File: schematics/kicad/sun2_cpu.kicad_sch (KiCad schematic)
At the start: 9 parts, among them U100 MC68010, U111 74F251, U115 74F04, U119 74LS148, U120 8211

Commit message: Substantial work on first page/CPU
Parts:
- added C100: C, symbol Device:C
- added R100, R102: 16k, symbol Device:R_US
- added R101: 100k, symbol Device:R_US
- added R103: 6.8k, symbol Device:R_US
- added U102: 74F00, Package_DIP:DIP-14_W7.62mm, symbol sun2:74F00
- added U109: 74F08, Package_DIP:DIP-14_W7.62mm, symbol sun2:74F08
- added U110: 7407, Package_DIP:DIP-14_W7.62mm, symbol sun2:7407
- added U114: 74LS20, symbol 74xx:74LS20
- added U122: 7406, Package_DIP:DIP-14_W7.62mm, symbol sun2:7406
- added U206: 74F74, Package_DIP:DIP-14_W7.62mm, symbol sun2:74F74
- added U608, U610: 74LS04, symbol sun2:74LS04
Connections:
- net P.D4: now reaches U100.1 (D4)
- net P.DTACK\: now reaches U100.10 (~{DTACK})
- net P.DTACK\: now also U111.6 (W)
- net P.BG\: now reaches U100.11 (~{BG})
- net P.BACK\: now reaches U100.12 (~{BGACK})
- net P.BR\: now reaches U100.13 (~{BR})
- net VCC: now reaches U100.14 (V_{CC})
- net VCC: now also S100.1 (common), S103.1 (common), S104.1 (common), S105.1 (common), U100.49 (V_{CC}), U119.16 (VCC), U120.8 (VCC), R100.1, U206.1 (~{R})
- net C(100.0-50): now reaches U100.15 (CLK)
- net C(100.0-50): now also U206.3 (C)
- net GND: now reaches U100.16 (GND)
- net GND: now also U100.53 (GND), U119.10 (IO), U119.8 (GND), U120.5 (GND), C100.2, R103.2
- net P.HALT\: now reaches U100.17 (~{HALT})
- net P.HALT\: now also U110.2, U110.4
- net P.RESET\: now reaches U100.18 (~{RESET})
- net P.RESET\: now also U110.6, U608.9
- net P.D3: now reaches U100.2 (D3)
- net P.VPA\: now reaches U100.21 (~{VPA})
- net P.BERR\: now reaches U100.22 (~{BERR})
- net P.BERR\: now also U109.3
- net IPL2\: now reaches U100.23 (~{IPL2}), U119.6 (S2)
- net IPL1\: now reaches U100.24 (~{IPL1}), U119.7 (S1)
- net IPL0\: now reaches U100.25 (~{IPL0}), U119.9 (S0)
- net P.FC2: now reaches U100.26 (FC2)
- net P.FC2: now also S104.4 (R3)
- net P.FC1: now reaches U100.27 (FC1)
- net P.FC1: now also S104.3 (R2)
- net P.FC0: now reaches U100.28 (FC0)
- net P.FC0: now also S104.2 (R1)
- net P.A1: now reaches U100.29 (A1)
- net P.D2: now reaches U100.3 (D2)
- net P.A2: now reaches U100.30 (A2)
- net P.A3: now reaches U100.31 (A3)
- net P.A4: now reaches U100.32 (A4)
- net P.A5: now reaches U100.33 (A5)
- net P.A6: now reaches U100.34 (A6)
- net P.A7: now reaches U100.35 (A7)
- net P.A8: now reaches U100.36 (A8)
- net P.A9: now reaches U100.37 (A9)
- net P.A10: now reaches U100.38 (A10)
- net P.A11: now reaches U100.39 (A11)
- net P.A11: now also S104.10 (R9)
- net P.D1: now reaches U100.4 (D1)
- net P.A12: now reaches U100.40 (A12)
- net P.A12: now also S104.9 (R8)
- net P.A13: now reaches U100.41 (A13)
- net P.A13: now also S104.8 (R7)
- net P.A14: now reaches U100.42 (A14)
- net P.A14: now also S104.7 (R6)
- net P.A15: now reaches U100.43 (A15)
- net P.A15: now also S105.10 (R9)
- net P.A16: now reaches U100.44 (A16)
- net P.A16: now also S105.9 (R8)
- net P.A17: now reaches U100.45 (A17)
- net P.A17: now also S105.8 (R7)
- net P.A18: now reaches U100.46 (A18)
- net P.A18: now also S105.7 (R6)
- net P.A19: now reaches U100.47 (A19)
- net P.A19: now also S105.6 (R5)
- net P.A20: now reaches U100.48 (A20)
- net P.A20: now also S105.5 (R4)
- net P.D0: now reaches U100.5 (D0)
- net P.A21: now reaches U100.50 (A21)
- net P.A21: now also S105.4 (R3)
- net P.A22: now reaches U100.51 (A22)
- net P.A22: now also S105.3 (R2)
- net P.A23: now reaches U100.52 (A23)
- net P.A23: now also S105.2 (R1)
- net P.D15: now reaches U100.54 (D15)
- net P.D14: now reaches U100.55 (D14)
- net P.D13: now reaches U100.56 (D13)
- net P.D12: now reaches U100.57 (D12)
- net P.D11: now reaches U100.58 (D11)
- net P.D10: now reaches U100.59 (D10)
- net P.AS\: now reaches U100.6 (~{AS})
- net P.AS\: now also U111.7 (S), U115.1
- net P.D9: now reaches U100.60 (D9)
- net P.D8: now reaches U100.61 (D8)
- net P.D7: now reaches U100.62 (D7)
- net P.D6: now reaches U100.63 (D6)
- net P.D5: now reaches U100.64 (D5)
- net P.UDS\: now reaches U100.7 (~{UDS})
- net P.UDS\: now also U115.3, U109.5
- net P.LDS\: now reaches U100.8 (~{LDS})
- net P.LDS\: now also U115.5, U109.4
- net P.R/W\: now reaches U100.9 (R/~{W})
- net P.R/W\: now also U115.9
- net Q.AS\: now reaches U115.12
- net AS: now reaches U115.13
- net AS: now also U115.2
- net XACK: now reaches U115.10
- net XACK: now also U111.12 (D7), U111.13 (D6)
- net XACK\: now reaches U115.11
- net INT4\: now reaches U119.1 (I4)
- net INT4\: now also S100.6 (R5)
- net INT1\: now reaches U119.11 (I1)
- net INT1\: now also S100.3 (R2)
- net INT2\: now reaches U119.12 (I2)
- net INT2\: now also S100.4 (R3)
- net INT3\: now reaches U119.13 (I3)
- net INT3\: now also S100.5 (R4)
- net INT5\: now reaches U119.2 (I5)
- net INT5\: now also S100.7 (R6)
- net INT6\: now reaches U119.3 (I6)
- net INT6\: now also S100.8 (R7)
- net INT7\: now reaches U119.4 (I7)
- net INT7\: now also S100.2 (R1)
- net at U119.5 (EI): now also U608.12
- net C.S5: now reaches U111.1 (D3)
- net C.S5: now also U111.4 (D0)
- net TYPE1: now reaches U111.10 (B)
- net TYPE0: now reaches U111.11 (A)
- net IOACK: now reaches U111.14 (D5)
- net P2.WAIT\: now reaches U111.15 (D4)
- net P2.WAIT\: now also U122.4
- net C.S4: now reaches U111.9 (C)
- net LDS: now reaches U115.6
- net R\/W: now reaches U115.8
- net UDS: now reaches U115.4
- net POR\: now reaches S104.5 (R4)
- net POR\: now also U120.4 (OUT)
- net EN.PARGEN\: now reaches S104.6 (R5)
- net FPPERR\: now reaches S100.10 (R9)
- net INT.SCC\: now reaches S100.9 (R8)
- net at U120.2 (HYS): now also R101.2
- net at U120.3 (THR): now also R101.1, R102.2
- new net: C100.1, R100.2, R102.1, R103.1
- new net: U109.8, U122.3
- new net: U109.9, U610.12
- new net BERR: U206.6 (~{Q})
- new net BERR\: U109.1, U206.5 (Q)
- new net DS\: U109.6
- new net EN.INT: U608.13
- new net EN.S4: U102.13
- new net ERR: U102.12, U114.6
- new net ERR\: U102.11, U206.2 (D)
- new net INIT\: U110.3, U110.5
- new net OE.ROP\: U109.10
- new net P1.INIT\: U122.1, U608.8
- new net PARERRL\: U114.4
- new net PARERRU\: U114.5
- new net PROTERR\: U114.1
- new net RESET: U122.2
- new net ROPCYC\: U610.13
- new net TIMEOUT\: U114.2
- new net XBERR\: U109.2
- new net XHALT\: U110.1
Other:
- moved on the sheet: S100, U111A, U111B, U115A, U115B, U115C, U115D, U115E, U115F, U115G

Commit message: Finish first page/CPU
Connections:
- net C.S5: now also U111.2 (D2), U111.3 (D1)
- net FPPERR\: now also U110.13
- net INT.SCC\: now also U110.11
- net INT1\: now also U110.12, U122.8
- net INT2\: now also U122.10
- net INT3\: now also U122.12
- net INT6\: now also U110.10
- net P.AS\: now also S103.2 (R1)
- net P.BG\: now also S103.10 (R9)
- net P.DTACK\: now also S103.7 (R6)
- net P.HALT\: now also S103.6 (R5)
- net P.LDS\: now also S103.4 (R3)
- net P.RESET\: now also S103.8 (R7)
- net P.R/W\: now also S103.5 (R4)
- net P.UDS\: now also S103.3 (R2)
- net RESET: now also S103.9 (R8)
- net EN.INT2: now reaches U122.11
- net EN.INT3: now reaches U122.13
- net EN.INT1: now reaches U122.9
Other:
- note added: "BERR LOGIC"
- note added: "DTACK GENERATOR"
- note added: "INTERRUPT LOGIC"
- note added: "POWER-ON RESET"
- moved on the sheet: C100, R100, R101, R102, R103, S103, S104, S105, U100, U102D, U109A, U109B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

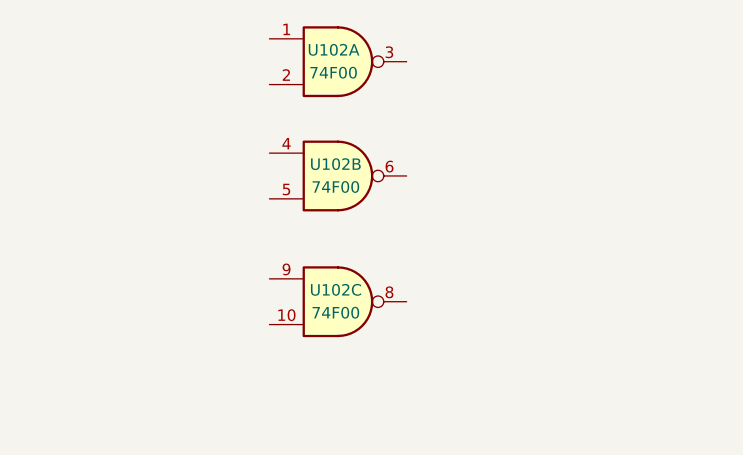
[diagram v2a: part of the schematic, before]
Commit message: System clock generator
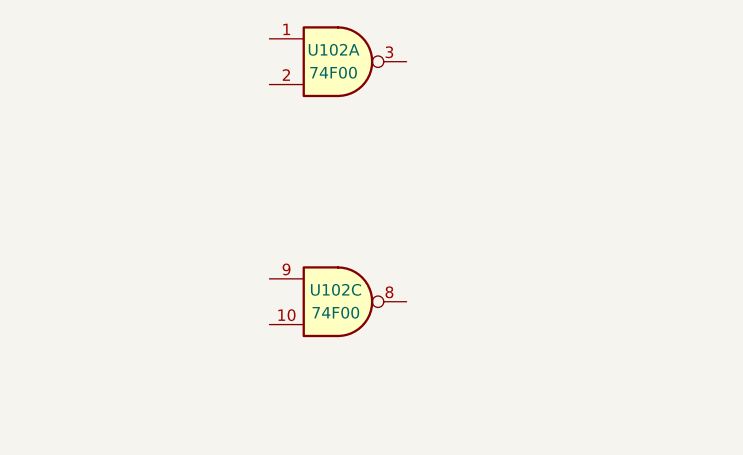
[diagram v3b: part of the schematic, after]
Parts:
- removed unit 2 of U102
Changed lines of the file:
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@@
-	)
-	(symbol
-		(lib_id "sun2:74F00")
-		(at -40.64 12.7 0)
-		(unit 2)
-		(exclude_from_sim no)
-		(in_bom yes)
-		(on_board yes)
-		(dnp no)
-		(property "Reference" "U102"
-			(at -40.894 11.43 0)
-			(effects
-				(font
-					(size 1.27 1.27)
-				)
-			)
-		)
-		(property "Value" "74F00"
-			(at -40.894 13.97 0)
-			(effects
-				(font
-					(size 1.27 1.27)
-				)
-			)
-		)
-		(property "Footprint" "Package_DIP:DIP-14_W7.62mm"
-			(at -40.64 12.7 0)
-			(effects
-				(font
-					(size 1.27 1.27)
-				)
-				(hide yes)
-			)
-		)
-		(property "Datasheet" "https://www.ti.com/lit/ds/symlink/sn74f00.pdf"
-			(at -40.64 12.7 0)
-			(effects
-				(font
-					(size 1.27 1.27)
-				)
-				(hide yes)
-			)
-		)
-		(property "Description" "quad 2-input NAND gate"
-			(at -40.64 12.7 0)
-			(effects
-				(font
-					(size 1.27 1.27)
-				)
-				(hide yes)
-			)
-		)
-		(property "Order Link" "https://www.digikey.com/en/products/detail/texas-instruments/SN74F00N/373665"
-			(at -40.64 12.7 0)
-			(effects
-				(font
-					(size 1.27 1.27)
-				)
-				(hide yes)
-			)
-		)
-		(pin "4"
-		)
-		(pin "9"
-		)
-		(pin "5"
-		)
-		(pin "6"
-		)
-		(pin "13"
-		)
-		(pin "11"
-		)
-		(pin "3"
-		)
-		(pin "1"
-		)
-		(pin "2"
-		)
-		(pin "12"
-		)
-		(pin "10"
-		)
-		(pin "8"
-		)
-		(pin "14"
-		)
-		(pin "7"
-		)
-		(instances
-			(project ""
-				(path "/67ee2072-0b57-4a50-8537-b17b5f651e89/2d3d381d-4c8b-4bfc-8adc-91fc2fe1e9d0"
-					(reference "U102")
-					(unit 2)
-				)
-			)
-		)
 	)
 	(symbol

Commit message: Finish page2: Clock, Timers, DVMA
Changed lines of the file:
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@@
-		)
-	)
-	(label "P.AS\\"
-		(at 156.21 128.27 0)
-		(effects
-			(font
-				(size 1.27 1.27)
-			)
-			(justify left bottom)
 		)
 	)
@@
 	)
 	(label "P.RESET\\"
-		(at 116.84 189.23 0)
+		(at 121.92 189.23 0)
 		(effects
 			(font
@@
 		)
 	)
-	(label "P.HALT\\"
-		(at 116.84 186.69 0)
-		(effects
-			(font
-				(size 1.27 1.27)
-			)
-			(justify left bottom)
+	(hierarchical_label "P.HALT\\"
+		(shape output)
+		(at 109.22 186.69 0)
+		(effects
+			(font
+				(size 1.27 1.27)
+			)
+			(justify left)
 		)
 	)
@@
 		(effects
 			(font
+				(size 1.27 1.27)
+			)
+			(justify left)
+		)
+	)
+	(hierarchical_label "P.AS\\"
+		(shape tri_state)
+		(at 156.21 128.27 0)
+		(effects
+			(font

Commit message: Finish MMU
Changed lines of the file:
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@@
-		)
-	)
-	(label "ERR\\"
-		(at 74.93 119.38 0)
-		(effects
-			(font
-				(size 1.27 1.27)
-			)
-			(justify left bottom)
 		)
 	)
@@
 		(effects
 			(font
+				(size 1.27 1.27)
+			)
+			(justify left)
+		)
+	)
+	(hierarchical_label "ERR\\"
+		(shape output)
+		(at 74.93 116.84 0)
+		(effects
+			(font

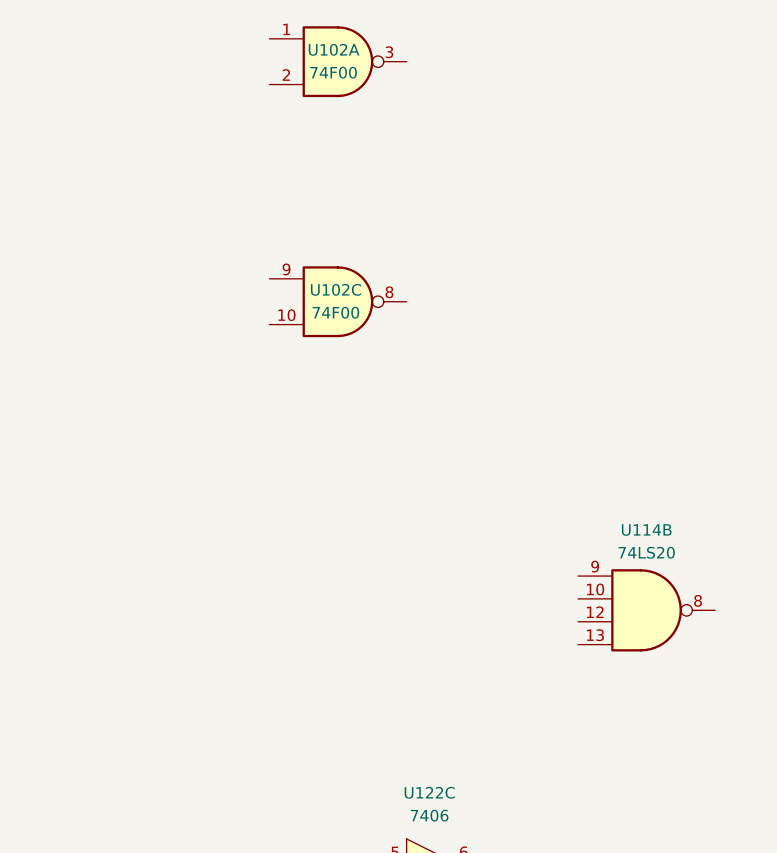
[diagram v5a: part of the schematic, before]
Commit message: PROM, RTC, Registers work
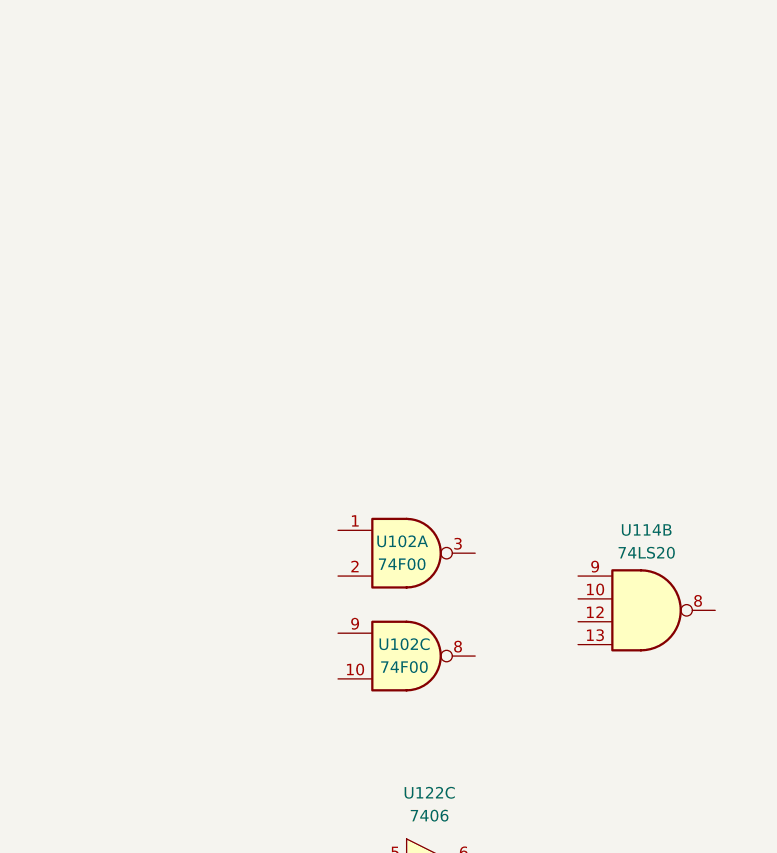
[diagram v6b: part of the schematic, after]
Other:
- moved on the sheet: U102A, U102C
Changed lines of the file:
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@@
 	(symbol
 		(lib_id "sun2:74F00")
-		(at -40.64 26.67 0)
+		(at -33.02 66.04 0)
 		(unit 3)
 		(exclude_from_sim no)
@@
 		(dnp no)
 		(property "Reference" "U102"
-			(at -40.894 25.4 0)
+			(at -33.274 64.77 0)
 			(effects
 				(font
@@
 		)
 		(property "Value" "74F00"
-			(at -40.894 27.94 0)
+			(at -33.274 67.31 0)
 			(effects
 				(font
@@
 		)
 		(property "Footprint" "Package_DIP:DIP-14_W7.62mm"
-			(at -40.64 26.67 0)
+			(at -33.02 66.04 0)
 			(effects
 				(font
@@
 		)
 		(property "Datasheet" "https://www.ti.com/lit/ds/symlink/sn74f00.pdf"
-			(at -40.64 26.67 0)
+			(at -33.02 66.04 0)
 			(effects
 				(font
@@
 		)
 		(property "Description" "quad 2-input NAND gate"
-			(at -40.64 26.67 0)
+			(at -33.02 66.04 0)
 			(effects
 				(font
@@
 		)
 		(property "Order Link" "https://www.digikey.com/en/products/detail/texas-instruments/SN74F00N/373665"
-			(at -40.64 26.67 0)
+			(at -33.02 66.04 0)
 			(effects
 				(font
@@
 	(symbol
 		(lib_id "sun2:74F00")
-		(at -40.64 0 0)
+		(at -33.02 54.61 0)
 		(unit 1)
 		(exclude_from_sim no)
@@
 		(dnp no)
 		(property "Reference" "U102"
-			(at -41.148 -1.27 0)
+			(at -33.528 53.34 0)
 			(effects
 				(font
@@
 		)
 		(property "Value" "74F00"
-			(at -41.148 1.27 0)
+			(at -33.528 55.88 0)
 			(effects
 				(font
@@
 		)
 		(property "Footprint" "Package_DIP:DIP-14_W7.62mm"
-			(at -40.64 0 0)
+			(at -33.02 54.61 0)
 			(effects
 				(font
@@
 		)
 		(property "Datasheet" "https://www.ti.com/lit/ds/symlink/sn74f00.pdf"
-			(at -40.64 0 0)
+			(at -33.02 54.61 0)
 			(effects
 				(font
@@
 		)
 		(property "Description" "quad 2-input NAND gate"
-			(at -40.64 0 0)
+			(at -33.02 54.61 0)
 			(effects
 				(font
@@
 		)
 		(property "Order Link" "https://www.digikey.com/en/products/detail/texas-instruments/SN74F00N/373665"
-			(at -40.64 0 0)
+			(at -33.02 54.61 0)
 			(effects
 				(font

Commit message: Finish PROM, RTC, Registers
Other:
- moved on the sheet: U114A
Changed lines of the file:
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@@
 	(wire
 		(pts
-			(xy 55.88 114.3) (xy 59.69 114.3)
+			(xy 54.61 114.3) (xy 59.69 114.3)
 		)
 		(stroke
@@
 		)
 	)
-	(label "ERR"
-		(at 55.88 114.3 0)
-		(effects
-			(font
-				(size 1.27 1.27)
-			)
-			(justify left bottom)
-		)
-	)
 	(label "INT6\\"
 		(at 97.79 166.37 180)
@@
 		)
 	)
+	(hierarchical_label "ERR"
+		(shape output)
+		(at 54.61 114.3 0)
+		(effects
+			(font
+				(size 1.27 1.27)
+			)
+			(justify left)
+		)
+	)
 	(hierarchical_label "PARERRL\\"
 		(shape input)
-		(at 40.64 115.57 180)
+		(at 39.37 115.57 180)
 		(effects
 			(font
@@
 	(hierarchical_label "TIMEOUT\\"
 		(shape input)
-		(at 40.64 113.03 180)
+		(at 39.37 113.03 180)
 		(effects
 			(font
@@
 	(hierarchical_label "PARERRU\\"
 		(shape input)
-		(at 40.64 118.11 180)
+		(at 39.37 118.11 180)
 		(effects
 			(font
@@
 	(hierarchical_label "PROTERR\\"
 		(shape input)
-		(at 40.64 110.49 180)
+		(at 39.37 110.49 180)
 		(effects
 			(font
@@
 	(symbol
 		(lib_id "74xx:74LS20")
-		(at 48.26 114.3 0)
+		(at 46.99 114.3 0)
 		(unit 1)
 		(exclude_from_sim no)
@@
 		(dnp no)
 		(property "Reference" "U114"
-			(at 48.006 112.522 0)
+			(at 46.736 112.522 0)
 			(effects
 				(font
@@
 		)
 		(property "Value" "74LS20"
-			(at 48.006 115.062 0)
+			(at 46.736 115.062 0)
 			(effects
 				(font
@@
 		)
 		(property "Footprint" ""
-			(at 48.26 114.3 0)
+			(at 46.99 114.3 0)
 			(effects
 				(font
@@
 		)
 		(property "Datasheet" "http://www.ti.com/lit/gpn/sn74LS20"
-			(at 48.26 114.3 0)
+			(at 46.99 114.3 0)
 			(effects
 				(font
@@
 		)
 		(property "Description" "Dual 4-input NAND"
-			(at 48.26 114.3 0)
+			(at 46.99 114.3 0)
 			(effects
 				(font
